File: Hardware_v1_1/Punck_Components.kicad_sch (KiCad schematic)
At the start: 114 parts, among them J1 Conn_01x12_Female, J2 Conn_01x12_Female, J3 Conn_01x12_Female, J4 Conn_01x12_Female, J5 Debug_Header, J6 SWD_Header, J7 Eurorack_10_pin_power, Q1 MMBT3904, Q2 MMBT3904, Q3 MMBT3904, Q4 MMBT3904, Q5 MMBT3904, Q6 MMBT3904, Q7 MMBT3904, U1 TL074, U2 STM32H743ZITx, U3 W25Q128JVS, U4 PCM5100APW, U5 W25Q128JVS, U6 TPS561201, U7 LD1117-3.3-4Tab, Y1 8MHz 20pF

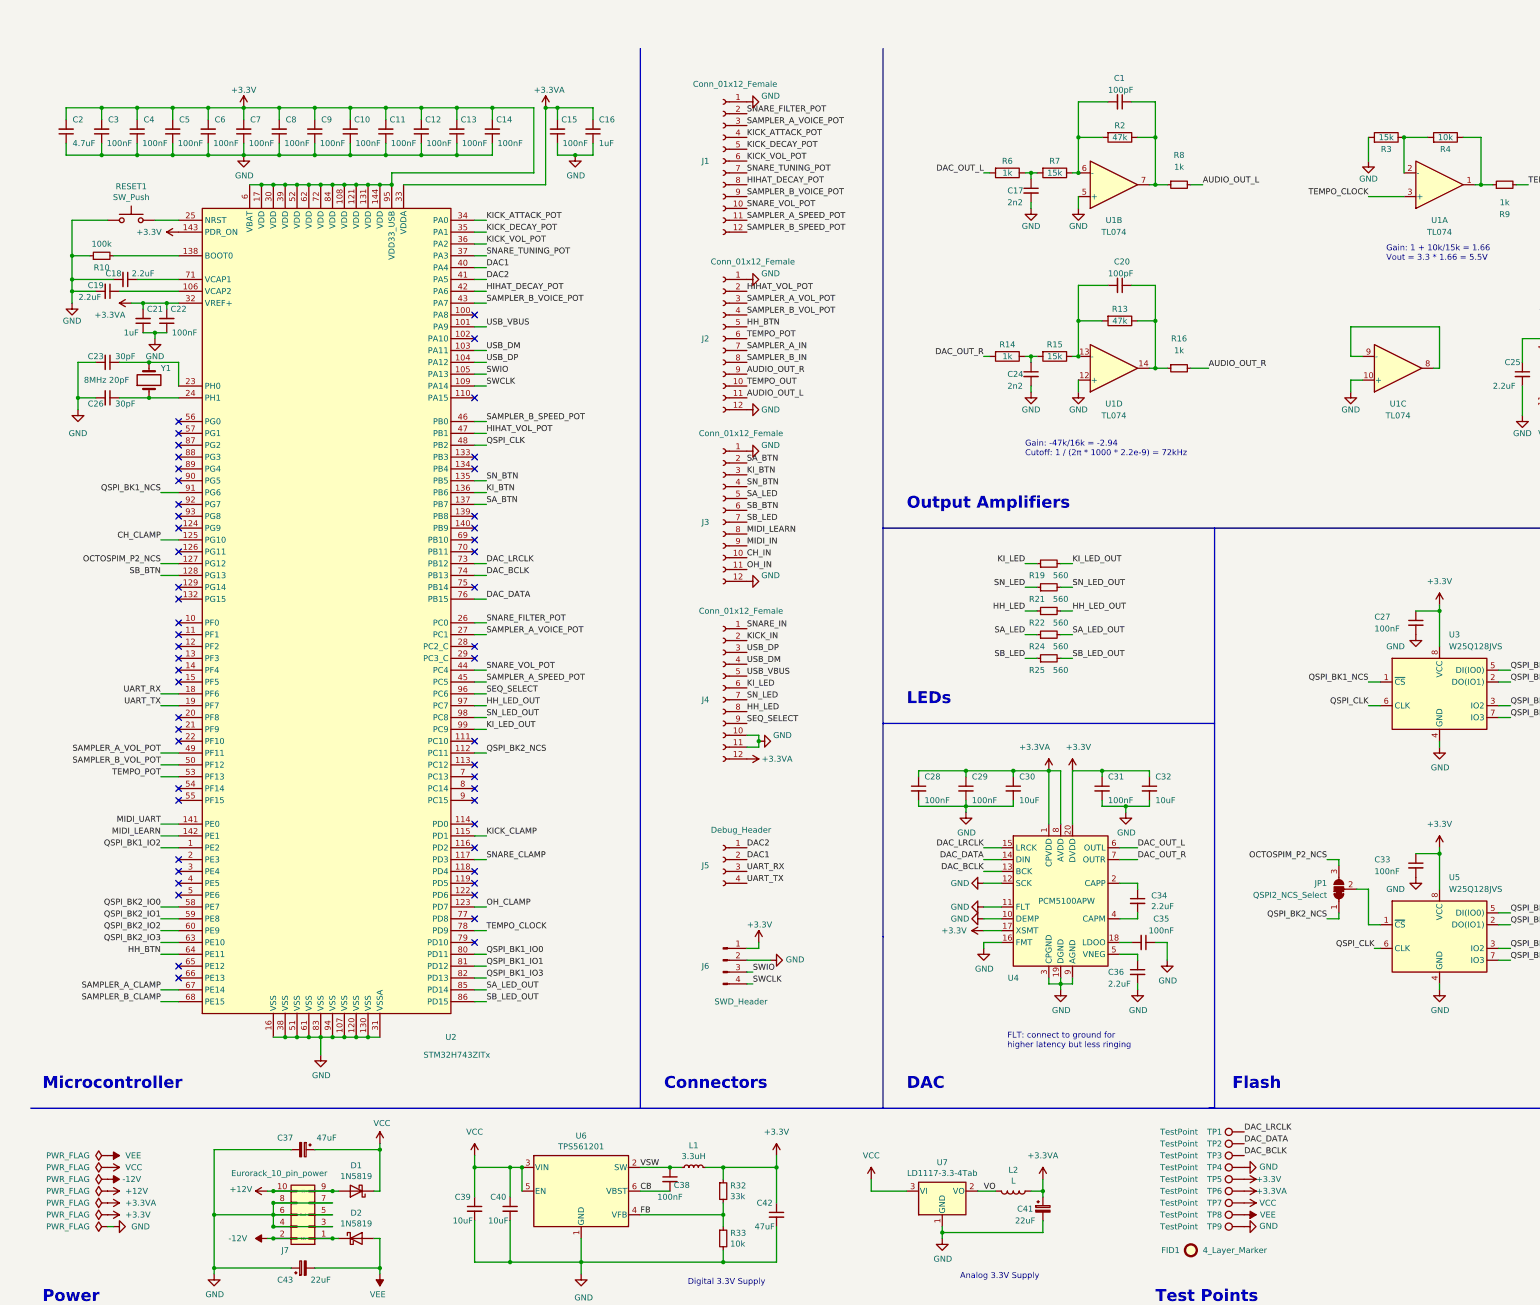
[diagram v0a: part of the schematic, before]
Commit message: Updated crystal to 12 MHz
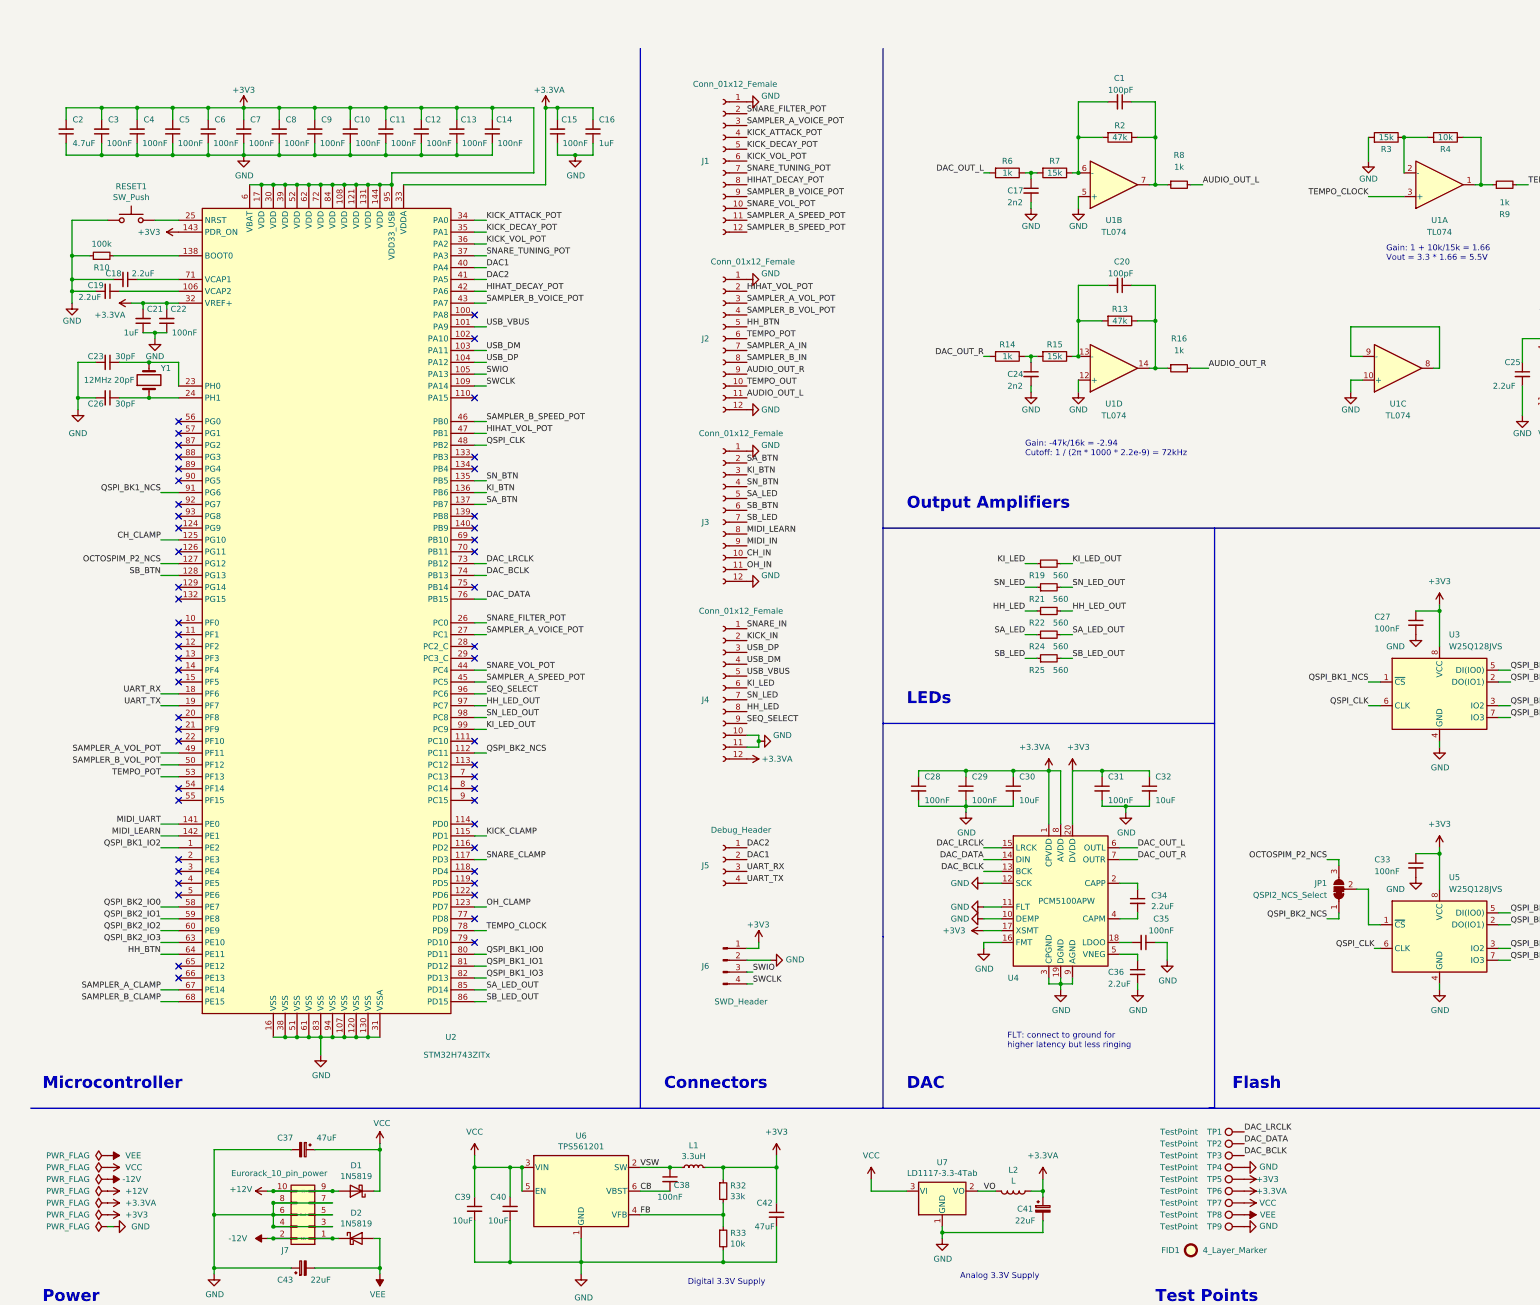
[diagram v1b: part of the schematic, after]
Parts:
- Y1: value 8MHz 20pF -> 12MHz 20pF
